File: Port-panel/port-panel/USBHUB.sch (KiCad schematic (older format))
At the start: 16 parts

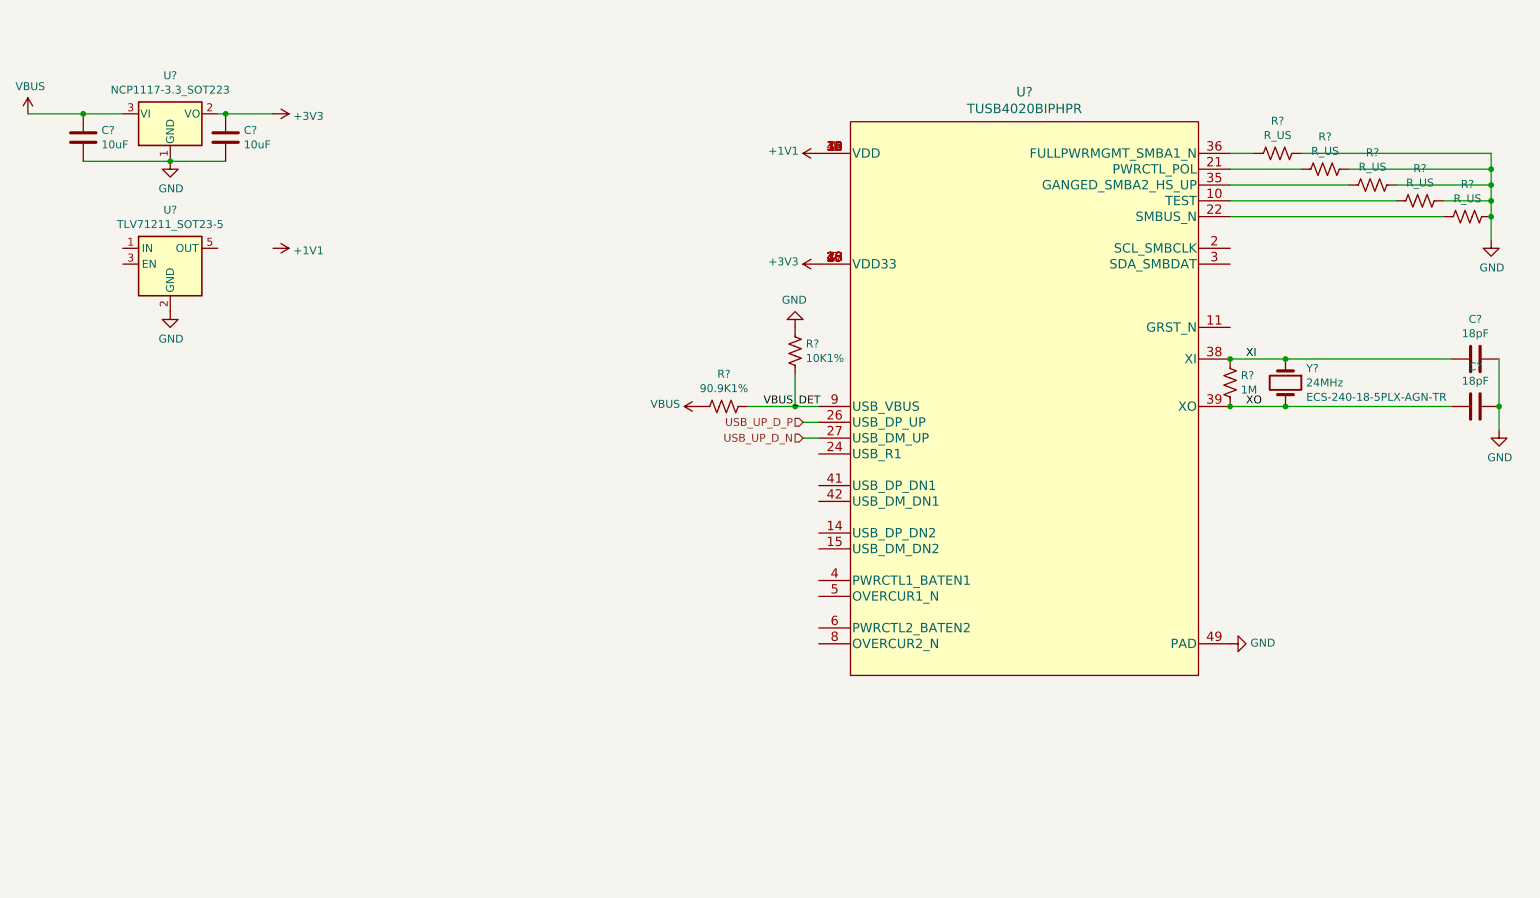
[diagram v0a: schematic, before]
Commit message: more port panel
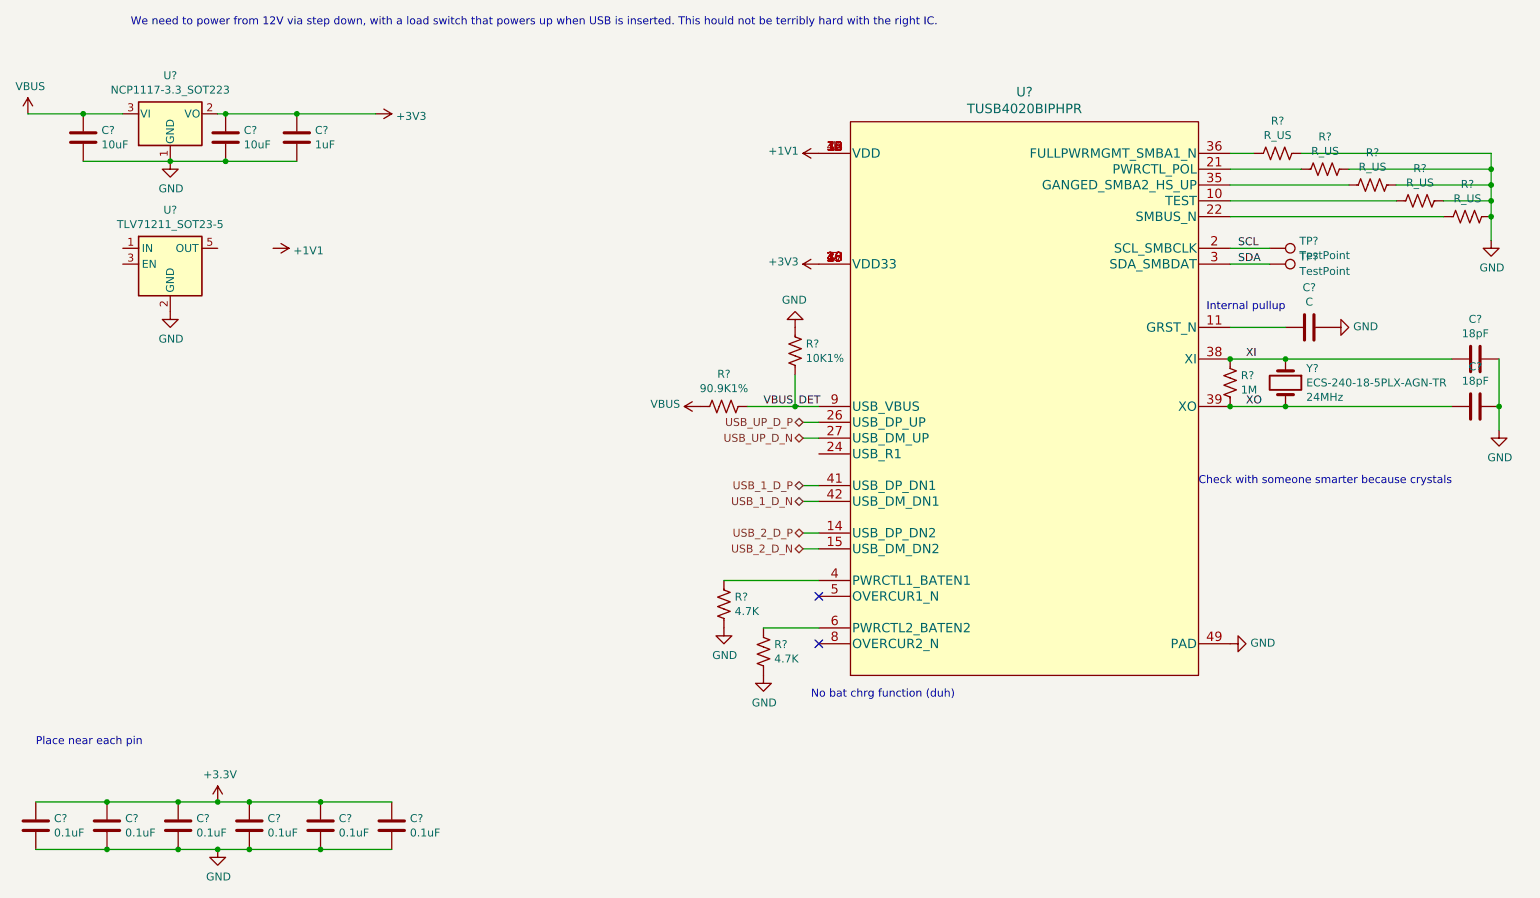
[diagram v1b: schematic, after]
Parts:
- added C?: C, symbol Device:C
- added C?: 1uF, symbol Device:C
- added C? (x6): 0.1uF, symbol Device:C
- added R? (x2): 4.7K, symbol Device:R_US
- added TP? (x2): TestPoint, symbol Connector:TestPoint
- Y?: value 24MHz -> ECS-240-18-5PLX-AGN-TR; Freq (none) -> 24MHz; Part Number ECS-240-18-5PLX-AGN-TR -> (none)
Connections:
- net +3V3: now also C?.1, C?.1, C?.1, C?.1, C?.1, C?.1, C?.1
- net GND: now also C?.1, C?.2, C?.2, C?.2, C?.2, C?.2, C?.2, C?.2, R?.2, R?.2
- net at U?.11 (GRST_N): now also C?.2
- net USB_2_D_P: now reaches U?.14 (USB_DP_DN2)
- net USB_2_D_N: now reaches U?.15 (USB_DM_DN2)
- net SCL: now reaches U?.2 (SCL_SMBCLK)
- net SCL: now also TP?.1
- net SDA: now reaches U?.3 (SDA_SMBDAT)
- net SDA: now also TP?.1
- net at U?.4 (PWRCTL1_BATEN1): now also R?.1
- net USB_1_D_P: now reaches U?.41 (USB_DP_DN1)
- net USB_1_D_N: now reaches U?.42 (USB_DM_DN1)
- net at U?.6 (PWRCTL2_BATEN2): now also R?.1
- no-connect marks 0 -> 2
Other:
- note added: "Check with someone smarter because crystals\n"
- note added: "Internal pullup"
- note added: "No bat chrg function (duh)"
- note added: "Place near each pin\n"
- note added: "We need to power from 12V via step down, with a load switch that powers up when USB is inserted. This hould not be terribly hard with the right IC."
